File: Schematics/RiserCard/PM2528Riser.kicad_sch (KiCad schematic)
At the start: 63 parts, among them K2 Conn_02x40_Odd_Even

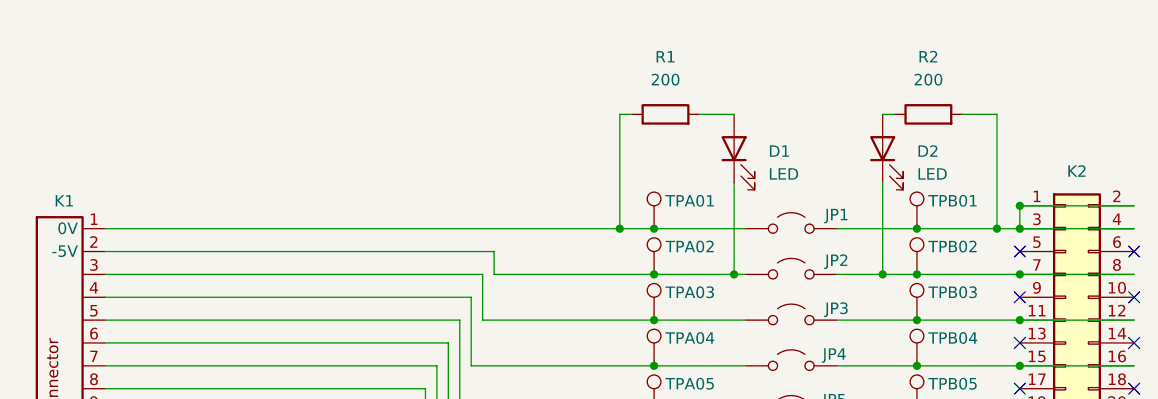
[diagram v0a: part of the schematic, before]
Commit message: Reworked N20/N21
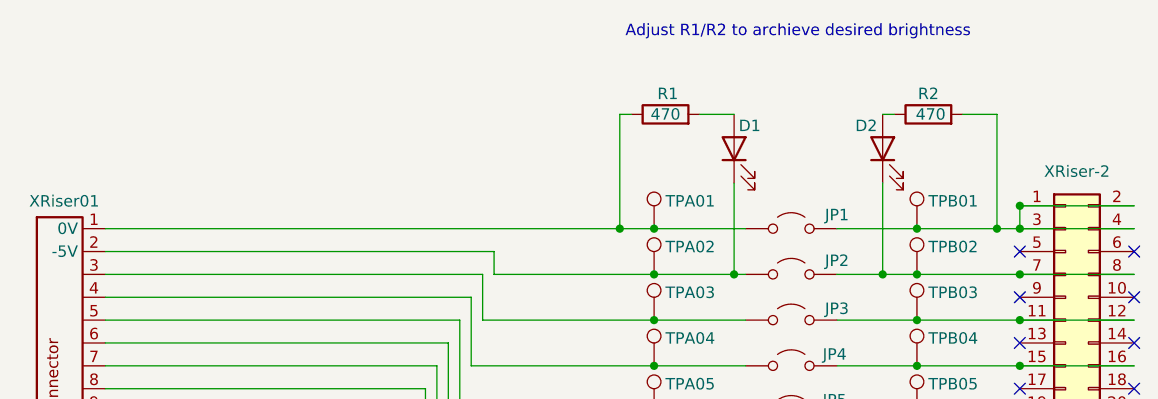
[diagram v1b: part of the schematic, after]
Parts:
- R1, R2: value 200 -> 470
- renumbered K2 to XRiser-2, K1 to XRiser01
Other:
- note added: "Adjust R1/R2 to archieve desired brightness"
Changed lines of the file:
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@@
 	(title_block
 		(title "PM2528 - Plugincard Riser")
-		(date "2024-10-04")
-		(rev "2.0")
+		(date "2025-08-06")
+		(rev "2.1")
 		(company "D. Kupers")
 	)
+	(text "Adjust R1/R2 to archieve desired brightness"
+		(exclude_from_sim no)
+		(at 160.782 30.226 0)
+		(effects
+			(font
+				(size 1.27 1.27)
+			)
+		)
+	)
 	(junction
 		(at 185.42 57.15)
@@
 		(on_board yes)
 		(dnp no)
-		(fields_autoplaced yes)
 		(property "Reference" "R1"
-			(at 146.05 33.02 90)
+			(at 146.304 37.084 90)
 			(effects
 				(font
@@
 			)
 		)
-		(property "Value" "200"
-			(at 146.05 35.56 90)
+		(property "Value" "470"
+			(at 146.05 39.37 90)
 			(effects
 				(font
@@
 		(on_board yes)
 		(dnp no)
-		(fields_autoplaced yes)
 		(property "Reference" "R2"
-			(at 175.26 33.02 90)
+			(at 175.26 37.084 90)
 			(effects
 				(font
@@
 			)
 		)
-		(property "Value" "200"
-			(at 175.26 35.56 90)
+		(property "Value" "470"
+			(at 175.514 39.37 90)
 			(effects
 				(font
@@
 		(on_board yes)
 		(dnp no)
-		(fields_autoplaced yes)
 		(property "Reference" "D2"
-			(at 173.99 43.4974 90)
+			(at 167.132 40.64 90)
 			(effects
 				(font
@@
 				)
 				(justify right)
+				(hide yes)
 			)
 		)
@@
 		(on_board yes)
 		(dnp no)
-		(property "Reference" "K1"
+		(property "Reference" "XRiser01"
 			(at 79.248 49.022 0)
 			(effects
@@
 			(project ""
 				(path "/f95ab724-7d1f-44cc-9992-5b2ce0fd0b2b"
-					(reference "K1")
+					(reference "XRiser01")
 					(unit 1)
 				)
@@
 		(on_board yes)
 		(dnp no)
-		(property "Reference" "K2"
+		(property "Reference" "XRiser-2"
 			(at 191.77 45.72 0)
 			(effects
@@
 			(project ""
 				(path "/f95ab724-7d1f-44cc-9992-5b2ce0fd0b2b"
-					(reference "K2")
+					(reference "XRiser-2")
 					(unit 1)
 				)
@@
 		(on_board yes)
 		(dnp no)
-		(fields_autoplaced yes)
 		(property "Reference" "D1"
-			(at 157.48 43.4974 90)
+			(at 154.178 40.64 90)
 			(effects
 				(font
@@
 				)
 				(justify right)
+				(hide yes)
 			)
 		)
